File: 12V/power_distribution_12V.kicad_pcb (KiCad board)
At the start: 4 copper layers, 85.2 x 56 mm, 35 parts, among them J1 39301020, J10 39301020, J11 39301020, J2 768250004, J20 1720650004, J3 39301020, J4 768250004, J6 39301020, J7 39301020, J9 39301020, U1 RASPBERRY_PI_4B_4GB

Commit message: corrected resistors for LEDs
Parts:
- R1, R2, R3, R4, R6, R7, R8: value 10k -> 5100
- R5: value 10k -> 500
- U1: value RASPBERRY_PI_4B_4GB -> RASPBERRY_PCB

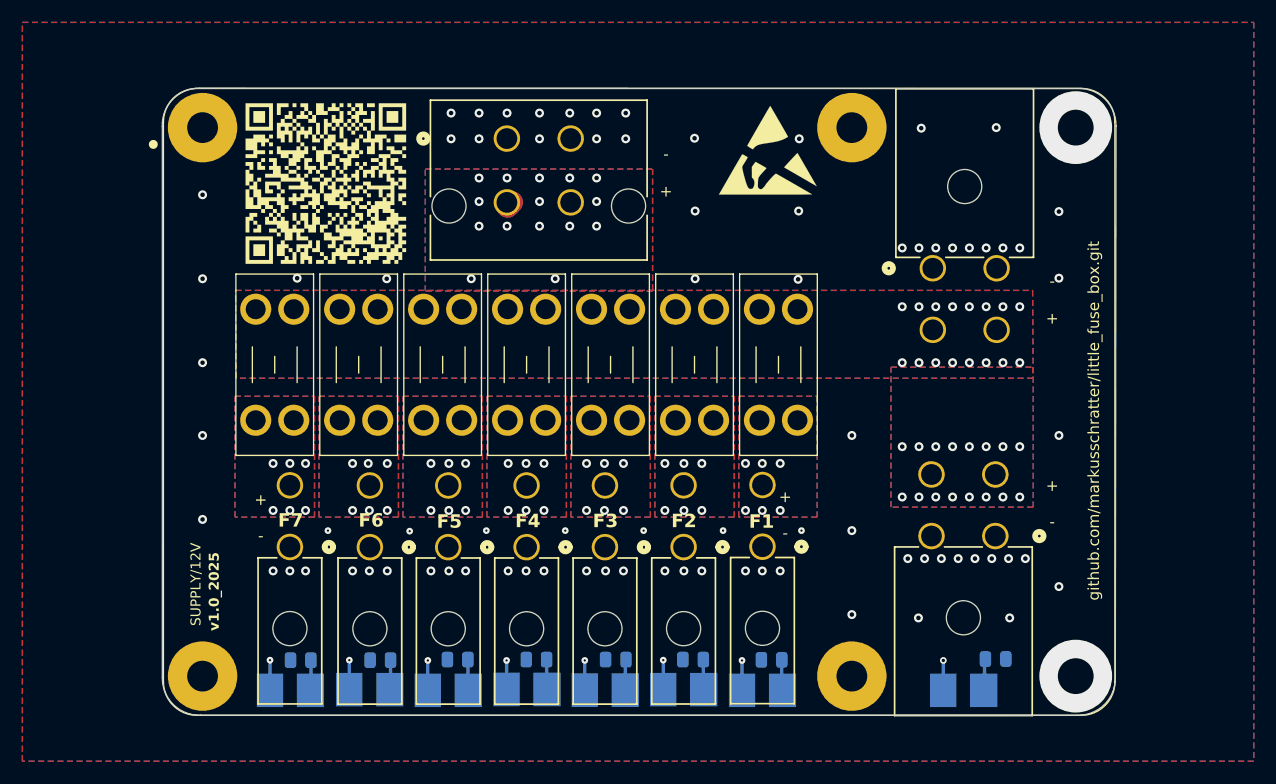
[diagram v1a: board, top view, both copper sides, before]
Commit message: changed layer priorities, increased drill hole sizes
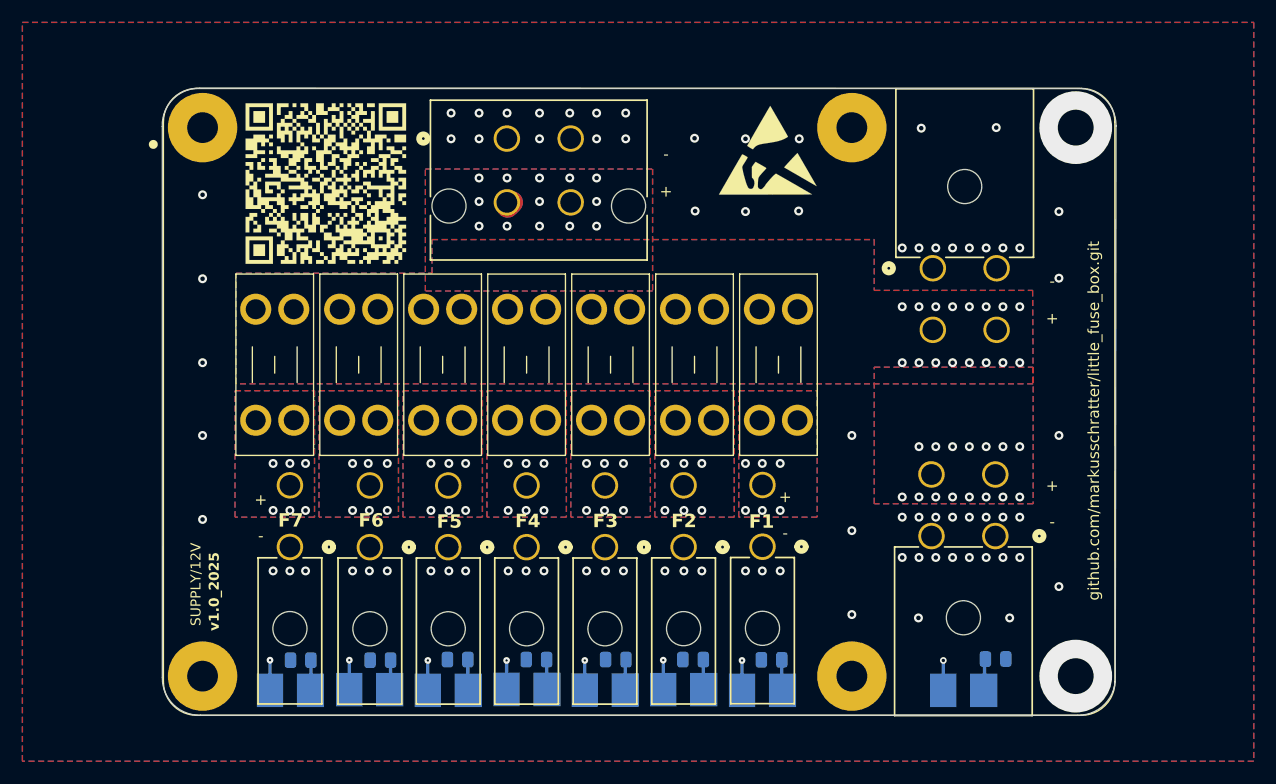
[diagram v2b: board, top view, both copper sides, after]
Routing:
- net VCC: vias 46 -> 45
- net GND: vias 82 -> 79

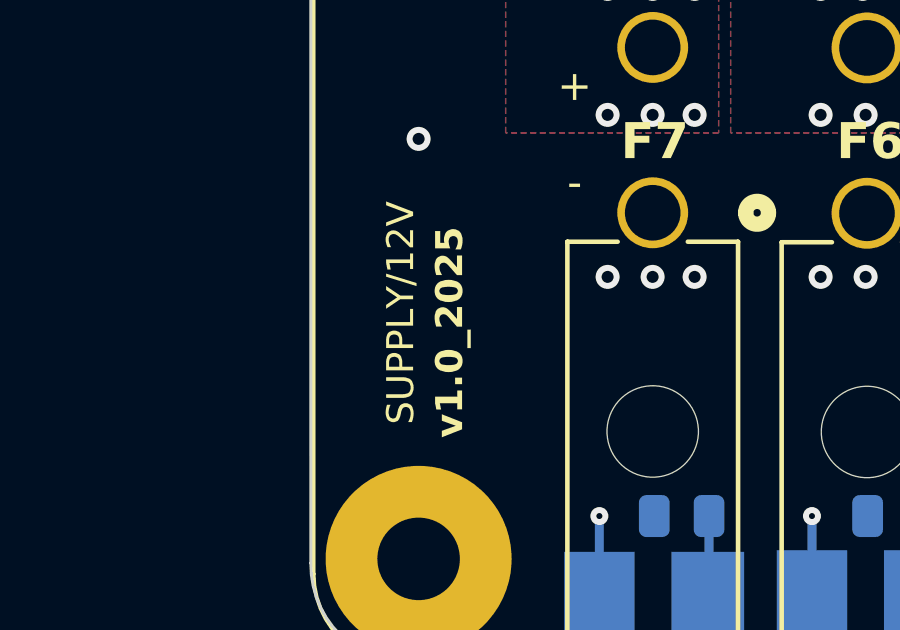
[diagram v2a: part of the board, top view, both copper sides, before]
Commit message: added 3d models to the pcbs
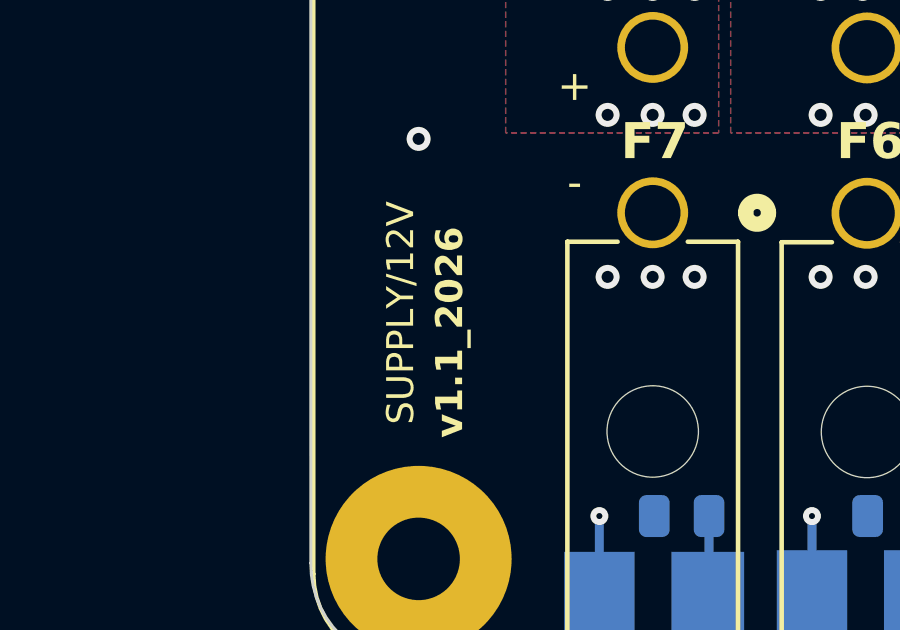
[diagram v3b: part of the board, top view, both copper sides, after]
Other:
- board text added: "v1.1_2026"
- board text removed: "v1.0_2025"
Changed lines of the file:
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@@
     (pad "2" thru_hole circle (at 0 -5.5118) (size 2.3622 2.3622) (drill 1.8542) (layers "*.Cu" "*.Mask")
       (net 16 "Net-(D7-Pad2)") (pintype "passive") (solder_mask_margin 0.102) (zone_connect 2))
+    (model "${KIPRJMOD}/3dmodels/39301020.step"
+      (offset (xyz 0 -13.9 0))
+      (scale (xyz 1 1 1))
+      (rotate (xyz 90 180 180))
+    )
   )
   (footprint "39301020:CONN_5569-02A_MOL" (layer "F.Cu")
@@
     (pad "2" thru_hole circle (at 0 -5.5118) (size 2.3622 2.3622) (drill 1.8542) (layers "*.Cu" "*.Mask")
       (net 4 "Net-(D1-Pad2)") (pintype "passive") (solder_mask_margin 0.102) (zone_connect 2))
+    (model "${KIPRJMOD}/3dmodels/39301020.step"
+      (offset (xyz 0 -13.9 0))
+      (scale (xyz 1 1 1))
+      (rotate (xyz 90 180 180))
+    )
   )
-  (footprint "RASPBERRY_PI_4B_4GB:MODULE_RASPBERRY_PI_4B_4GB" locked (layer "F.Cu")
+  (footprint "RASPBERRY_PI_4B_4GB:MODULE_RASPBERRY_PI_4B_4GB" (layer "F.Cu")
     (at 42.5 -28)
     (property "Availability" "Not in stock")
@@
     (fp_circle (center -43.4 -23) (end -43.2 -23)
       (stroke (width 0.4) (type solid)) (fill none) (layer "F.Fab"))
-    (pad "S1" thru_hole circle locked (at -39 -24.5) (size 6.2 6.2) (drill 2.75) (layers "*.Cu" "*.Mask")
+    (pad "S1" thru_hole circle (at -39 -24.5) (size 6.2 6.2) (drill 2.75) (layers "*.Cu" "*.Mask")
       (solder_mask_margin 0.102))
-    (pad "S2" thru_hole circle locked (at 19 -24.5) (size 6.2 6.2) (drill 2.75) (layers "*.Cu" "*.Mask")
+    (pad "S2" thru_hole circle (at 19 -24.5) (size 6.2 6.2) (drill 2.75) (layers "*.Cu" "*.Mask")
       (solder_mask_margin 0.102))
-    (pad "S3" thru_hole circle locked (at 19 24.5) (size 6.2 6.2) (drill 2.75) (layers "*.Cu" "*.Mask")
+    (pad "S3" thru_hole circle (at 19 24.5) (size 6.2 6.2) (drill 2.75) (layers "*.Cu" "*.Mask")
       (solder_mask_margin 0.102))
-    (pad "S4" thru_hole circle locked (at -39 24.5) (size 6.2 6.2) (drill 2.75) (layers "*.Cu" "*.Mask")
+    (pad "S4" thru_hole circle (at -39 24.5) (size 6.2 6.2) (drill 2.75) (layers "*.Cu" "*.Mask")
       (solder_mask_margin 0.102))
   )
@@
     (pad "2" thru_hole circle (at 0 -5.5118) (size 2.3622 2.3622) (drill 1.8542) (layers "*.Cu" "*.Mask")
       (net 10 "Net-(D4-Pad2)") (pintype "passive") (solder_mask_margin 0.102) (zone_connect 2))
+    (model "${KIPRJMOD}/3dmodels/39301020.step"
+      (offset (xyz 0 -13.9 0))
+      (scale (xyz 1 1 1))
+      (rotate (xyz 90 180 180))
+    )
   )
   (footprint "39301020:CONN_5569-02A_MOL" (layer "F.Cu")
@@
     (pad "2" thru_hole circle (at 0 -5.5118) (size 2.3622 2.3622) (drill 1.8542) (layers "*.Cu" "*.Mask")
       (net 6 "Net-(D2-Pad2)") (pintype "passive") (solder_mask_margin 0.102) (zone_connect 2))
+    (model "${KIPRJMOD}/3dmodels/39301020.step"
+      (offset (xyz 0 -13.9 0))
+      (scale (xyz 1 1 1))
+      (rotate (xyz 90 180 180))
+    )
   )
   (footprint "Fuse:Fuseholder_Blade_Mini_Keystone_3568" (layer "F.Cu")
@@
     (pad "2" thru_hole circle (at 0 -5.5118) (size 2.3622 2.3622) (drill 1.8542) (layers "*.Cu" "*.Mask")
       (net 12 "Net-(D5-Pad2)") (pintype "passive") (solder_mask_margin 0.102) (zone_connect 2))
+    (model "${KIPRJMOD}/3dmodels/39301020.step"
+      (offset (xyz 0 -13.9 0))
+      (scale (xyz 1 1 1))
+      (rotate (xyz 90 180 180))
+    )
   )
   (footprint "Fuse:Fuseholder_Blade_Mini_Keystone_3568" (layer "F.Cu")
@@
     (pad "4" thru_hole circle (at -5.700004 -5.499999 180) (size 2.3622 2.3622) (drill 1.8542) (layers "*.Cu" "*.Mask")
       (net 2 "VCC") (pinfunction "4") (pintype "unspecified") (zone_connect 2))
+    (model "${KIPRJMOD}/3dmodels/76825-0004.step"
+      (offset (xyz -25.2 -13.9 3))
+      (scale (xyz 1 1 1))
+      (rotate (xyz 90 180 0))
+    )
   )
   (footprint "Fuse:Fuseholder_Blade_Mini_Keystone_3568" (layer "F.Cu")
@@
     (pad "2" thru_hole circle (at 0 -5.5118) (size 2.3622 2.3622) (drill 1.8542) (layers "*.Cu" "*.Mask")
       (net 14 "Net-(D6-Pad2)") (pintype "passive") (solder_mask_margin 0.102) (zone_connect 2))
+    (model "${KIPRJMOD}/3dmodels/39301020.step"
+      (offset (xyz 0 -13.9 0))
+      (scale (xyz 1 1 1))
+      (rotate (xyz 90 180 180))
+    )
   )
   (footprint "mega_fit:CONN_SD-76825-0100_04_MOL" (layer "F.Cu")
@@
     (pad "4" thru_hole circle (at -5.700004 -5.499999) (size 2.3622 2.3622) (drill 1.8542) (layers "*.Cu" "*.Mask")
       (net 2 "VCC") (pinfunction "4") (pintype "unspecified") (zone_connect 2))
+    (model "${KIPRJMOD}/3dmodels/76825-0004.step"
+      (offset (xyz -25.2 -13.9 3))
+      (scale (xyz 1 1 1))
+      (rotate (xyz 90 180 0))
+    )
   )
   (footprint "mega_fit_stehend:CONN_SD-76829-0100_04_MOL" (layer "F.Cu")
@@
     (pad "4" thru_hole circle (at -5.700004 -5.700004 180) (size 2.3622 2.3622) (drill 1.8542) (layers "*.Cu" "*.Mask")
       (net 2 "VCC") (pinfunction "4") (pintype "unspecified") (zone_connect 2))
+    (model "${KIPRJMOD}/3dmodels/1720650004.step"
+      (offset (xyz -15.7 -0.4 13))
+      (scale (xyz 1 1 1))
+      (rotate (xyz 0 180 0))
+    )
   )
   (footprint "39301020:CONN_5569-02A_MOL" (layer "F.Cu")
@@
     (pad "2" thru_hole circle (at 0 -5.5118) (size 2.3622 2.3622) (drill 1.8542) (layers "*.Cu" "*.Mask")
       (net 8 "Net-(D3-Pad2)") (pintype "passive") (solder_mask_margin 0.102) (zone_connect 2))
+    (model "${KIPRJMOD}/3dmodels/39301020.step"
+      (offset (xyz 0 -13.9 0))
+      (scale (xyz 1 1 1))
+      (rotate (xyz 90 180 180))
+    )
   )
   (footprint "Fuse:Fuseholder_Blade_Mini_Keystone_3568" (layer "F.Cu")
@@
     (pad "2" smd rect (at 1.825 0 180) (size 2.35 3) (layers "B.Cu")
       (net 10 "Net-(D4-Pad2)") (pintype "passive"))
+    (model "${KIPRJMOD}/3dmodels/KA-4040SURSK.step"
+      (offset (xyz 0 1.5 2))
+      (scale (xyz 1 1 1))
+      (rotate (xyz -90 0 0))
+    )
   )
   (footprint "Resistor_SMD:R_0805_2012Metric" (layer "B.Cu")
@@
     (pad "2" smd rect (at 1.825 0 180) (size 2.35 3) (layers "B.Cu")
       (net 16 "Net-(D7-Pad2)") (pintype "passive"))
+    (model "${KIPRJMOD}/3dmodels/KA-4040SURSK.step"
+      (offset (xyz 0 1.5 2))
+      (scale (xyz 1 1 1))
+      (rotate (xyz -90 0 0))
+    )
   )
   (footprint "Resistor_SMD:R_0805_2012Metric" (layer "B.Cu")
@@
     (pad "2" smd rect (at 1.825 0 180) (size 2.35 3) (layers "B.Cu")
       (net 6 "Net-(D2-Pad2)") (pintype "passive"))
+    (model "${KIPRJMOD}/3dmodels/KA-4040SURSK.step"
+      (offset (xyz 0 1.5 2))
+      (scale (xyz 1 1 1))
+      (rotate (xyz -90 0 0))
+    )
   )
   (footprint "Resistor_SMD:R_0805_2012Metric" (layer "B.Cu")
@@
     (pad "2" smd rect (at 1.825 0 180) (size 2.35 3) (layers "B.Cu")
       (net 14 "Net-(D6-Pad2)") (pintype "passive"))
+    (model "${KIPRJMOD}/3dmodels/KA-4040SURSK.step"
+      (offset (xyz 0 1.5 2))
+      (scale (xyz 1 1 1))
+      (rotate (xyz -90 0 0))
+    )
   )
   (footprint "LS_A67K-J1L2-1-0-2-R33-Z:LED_LS_A67K-J1L2-1-0-2-R33-Z" (layer "B.Cu")
@@
     (pad "2" smd rect (at 1.825 0 180) (size 2.35 3) (layers "B.Cu")
       (net 8 "Net-(D3-Pad2)") (pintype "passive"))
+    (model "${KIPRJMOD}/3dmodels/KA-4040SURSK.step"
+      (offset (xyz 0 1.5 2))
+      (scale (xyz 1 1 1))
+      (rotate (xyz -90 0 0))
+    )
   )
   (footprint "LS_A67K-J1L2-1-0-2-R33-Z:LED_LS_A67K-J1L2-1-0-2-R33-Z" (layer "B.Cu")
@@
     (property "VERIFIER" "")
     (attr smd)
-    (fp_text reference "D8" (at -1.5 2.635) (layer "B.SilkS")
+    (fp_text reference "D8" (at -1.5 2.635) (layer "B.SilkS") hide
         (effects (font (size 1 1) (thickness 0.15)) (justify mirror))
     )
@@
     (pad "2" smd rect (at 1.825 0 180) (size 2.35 3) (layers "B.Cu")
       (net 2 "VCC") (pintype "passive"))
+    (model "${KIPRJMOD}/3dmodels/KA-4040SURSK.step"
+      (offset (xyz 0 1.5 2))
+      (scale (xyz 1 1 1))
+      (rotate (xyz -90 0 0))
+    )
   )
   (footprint "LS_A67K-J1L2-1-0-2-R33-Z:LED_LS_A67K-J1L2-1-0-2-R33-Z" (layer "B.Cu")
@@
     (pad "2" smd rect (at 1.825 0 180) (size 2.35 3) (layers "B.Cu")
       (net 12 "Net-(D5-Pad2)") (pintype "passive"))
+    (model "${KIPRJMOD}/3dmodels/KA-4040SURSK.step"
+      (offset (xyz 0 1.5 2))
+      (scale (xyz 1 1 1))
+      (rotate (xyz -90 0 0))
+    )
   )
   (footprint "Resistor_SMD:R_0805_2012Metric" (layer "B.Cu")
@@
     (pad "2" smd rect (at 1.825 0 180) (size 2.35 3) (layers "B.Cu")
       (net 4 "Net-(D1-Pad2)") (pintype "passive"))
+    (model "${KIPRJMOD}/3dmodels/KA-4040SURSK.step"
+      (offset (xyz 0 1.5 2))
+      (scale (xyz 1 1 1))
+      (rotate (xyz -90 0 0))
+    )
   )
   (footprint "Resistor_SMD:R_0805_2012Metric" (layer "B.Cu")
@@
     (effects (font (size 1.2 1.2) (thickness 0.2) bold) (justify left bottom))
   )
-  (gr_text "v1.0_2025" (at 5.059 -7.5344 90) (layer "F.SilkS")
+  (gr_text "v1.1_2026" (at 5.059 -7.5344 90) (layer "F.SilkS")
     (effects (font (size 0.9 0.9) (thickness 0.15) bold) (justify left bottom))
   )

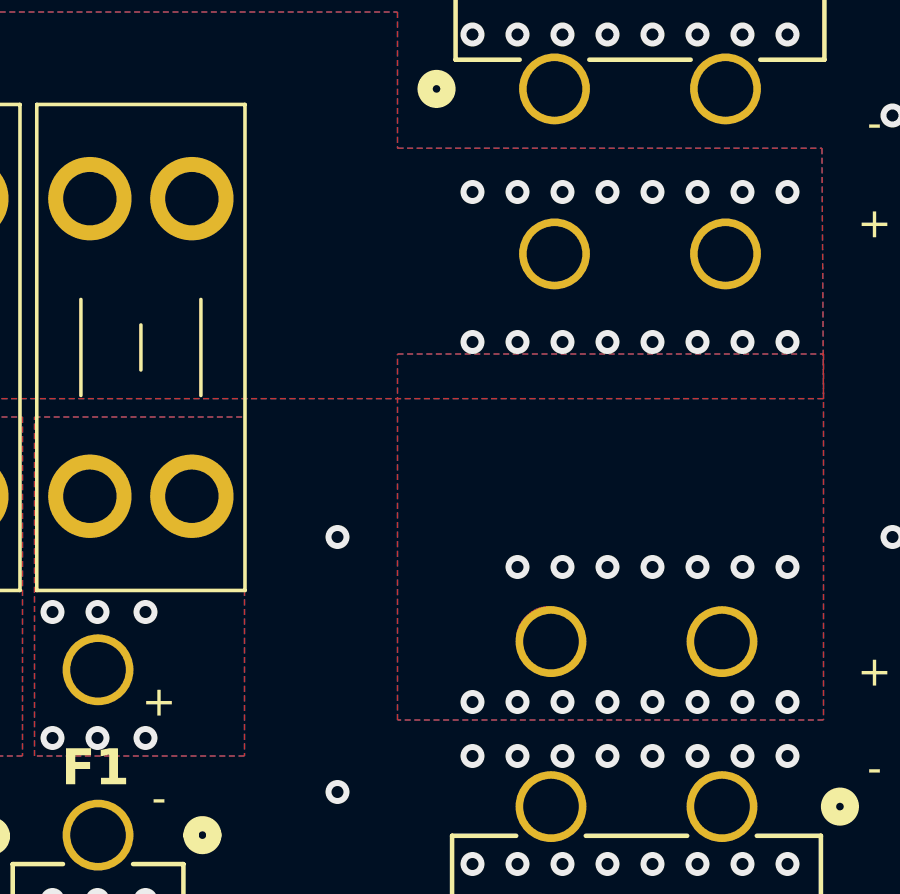
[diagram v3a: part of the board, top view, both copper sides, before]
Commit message: added 3d model of the board and changeg layer priorities
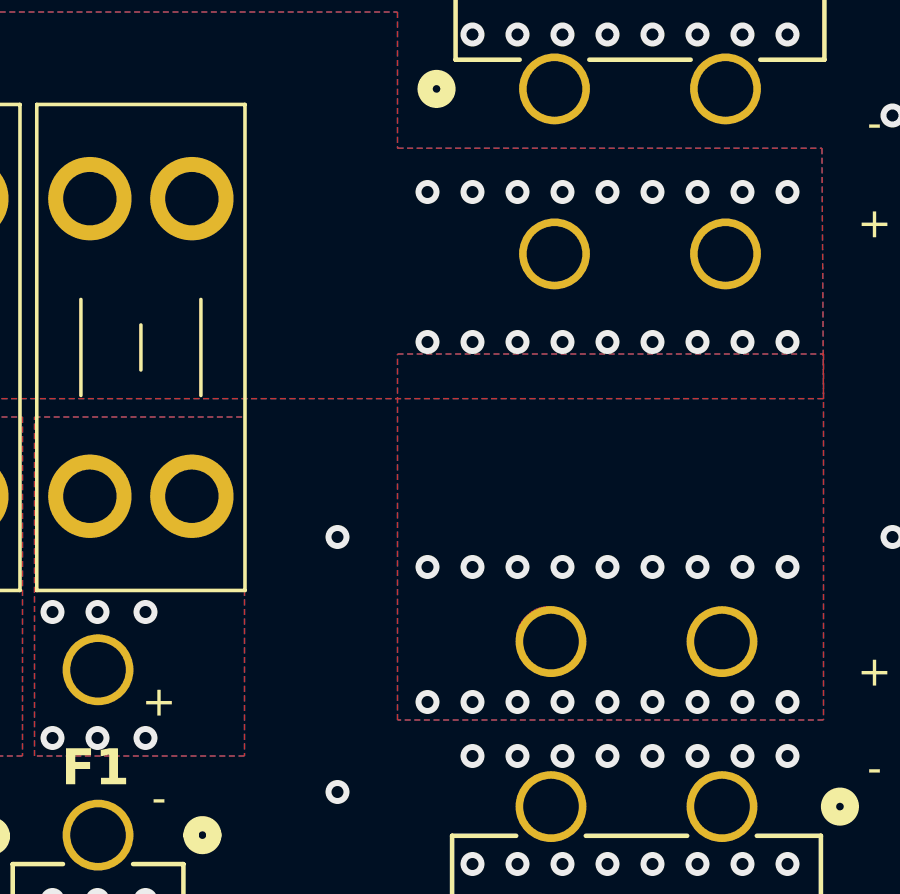
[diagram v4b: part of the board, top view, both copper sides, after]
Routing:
- net VCC: vias 45 -> 50
